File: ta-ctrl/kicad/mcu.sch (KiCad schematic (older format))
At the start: 11 parts, among them U6 MSP430FR5994IPM, Y1 32.768kHz, Y2 24MHz

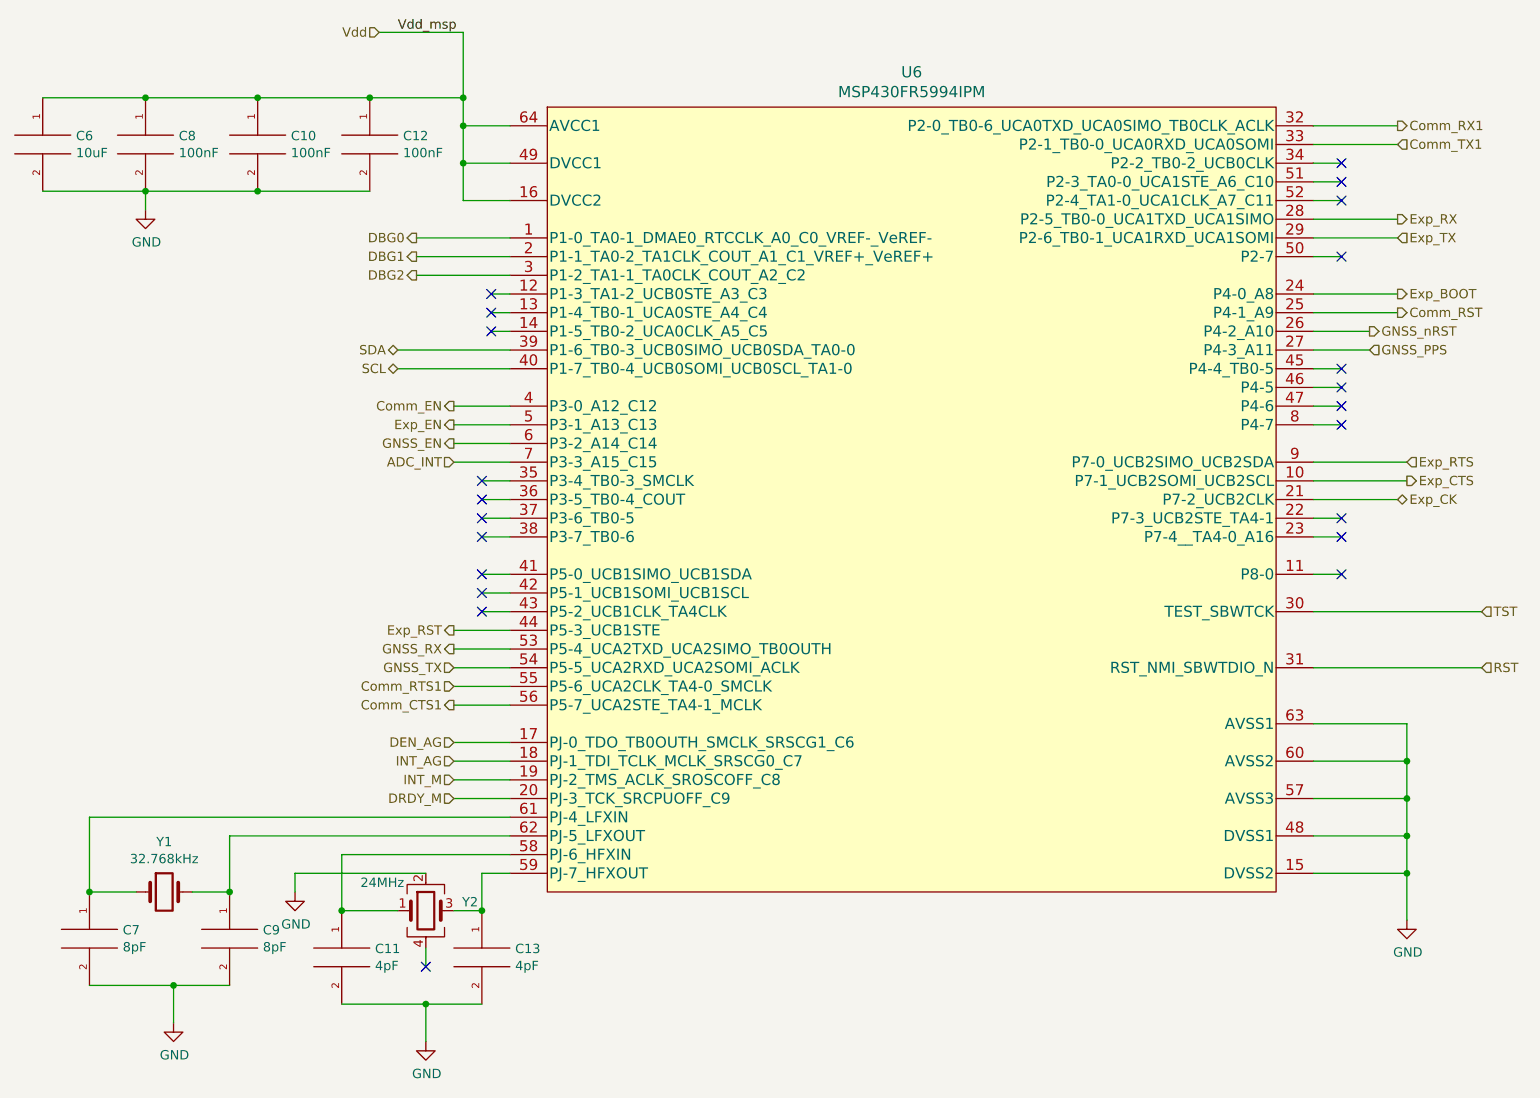
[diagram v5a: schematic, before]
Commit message: done routing except ground connections
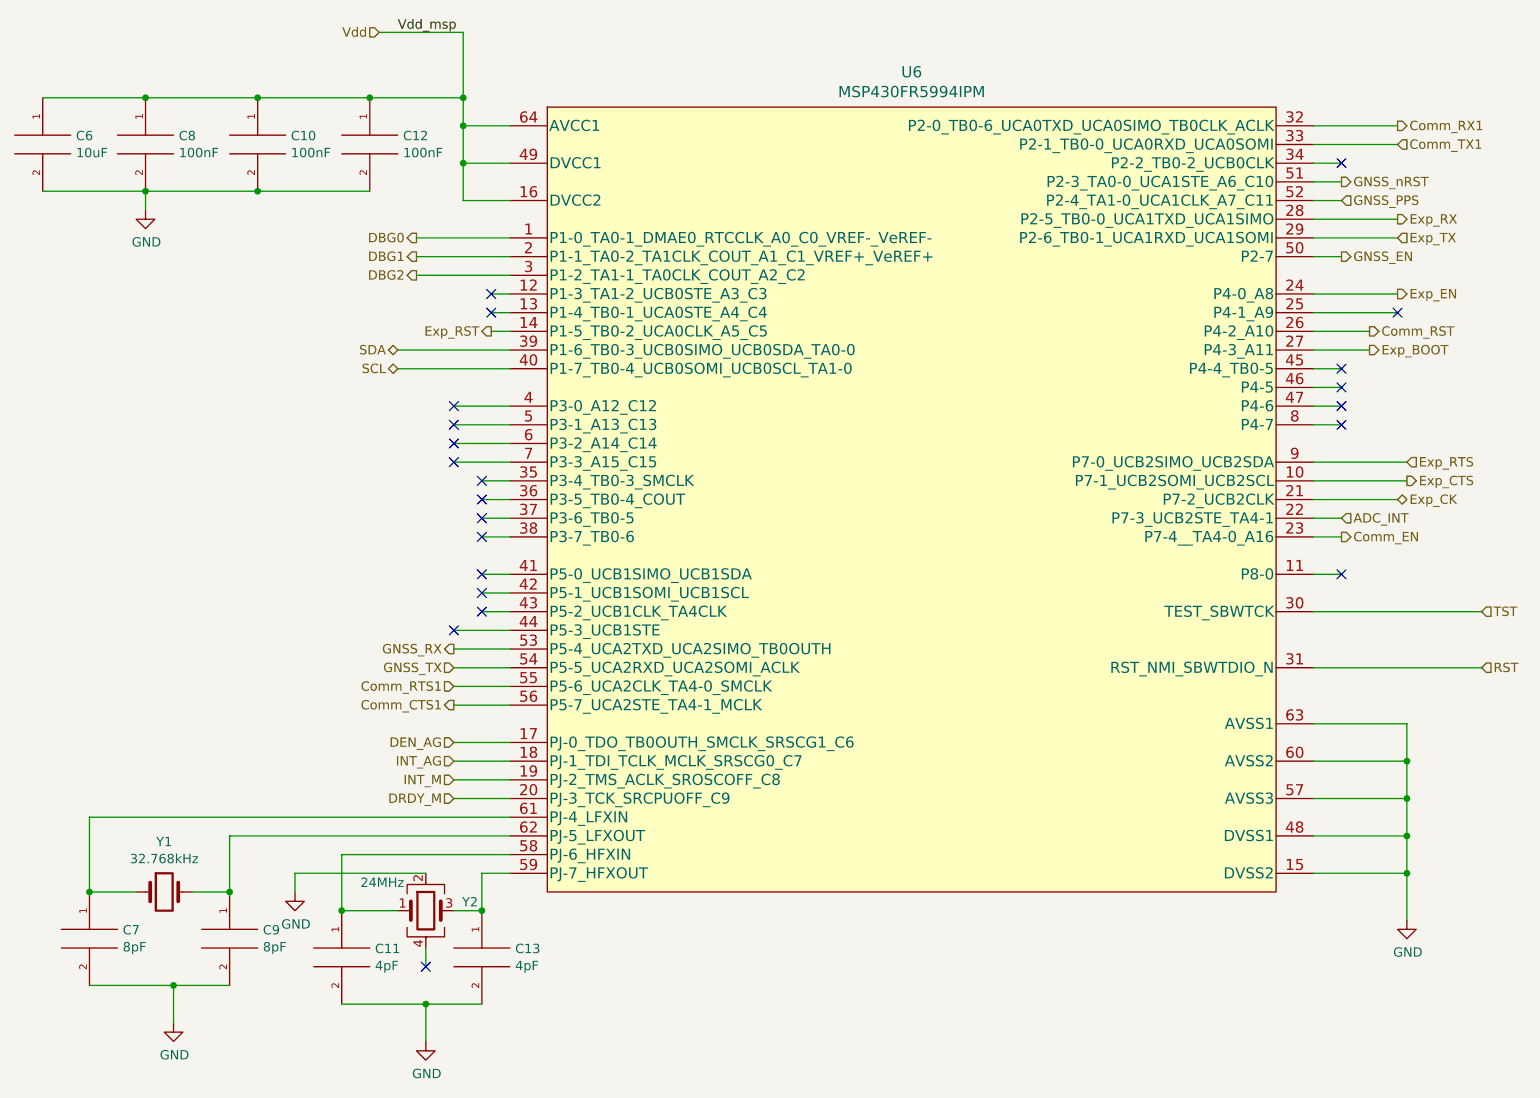
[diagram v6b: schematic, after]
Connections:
- net ADC_INT: now also U6.22 (P7-3_UCB2STE_TA4-1); no longer U6.7 (P3-3_A15_C15)
- net Comm_EN: now also U6.23 (P7-4__TA4-0_A16); no longer U6.4 (P3-0_A12_C12)
- net Comm_RST: now also U6.26 (P4-2_A10); no longer U6.25 (P4-1_A9)
- net Exp_BOOT: now also U6.27 (P4-3_A11); no longer U6.24 (P4-0_A8)
- net Exp_EN: now also U6.24 (P4-0_A8); no longer U6.5 (P3-1_A13_C13)
- net Exp_RST: now also U6.14 (P1-5_TB0-2_UCA0CLK_A5_C5); no longer U6.44 (P5-3_UCB1STE)
- net GNSS_EN: now also U6.50 (P2-7); no longer U6.6 (P3-2_A14_C14)
- net GNSS_PPS: now also U6.52 (P2-4_TA1-0_UCA1CLK_A7_C11); no longer U6.27 (P4-3_A11)
- net GNSS_nRST: now also U6.51 (P2-3_TA0-0_UCA1STE_A6_C10); no longer U6.26 (P4-2_A10)
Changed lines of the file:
@@
 Text HLabel 3050 4450 0    50   Input ~ 0
 GNSS_TX
-Text HLabel 7950 2650 2    50   Output ~ 0
+Text HLabel 7800 1850 2    50   Output ~ 0
 GNSS_nRST
-Text HLabel 7950 2750 2    50   Input ~ 0
+Text HLabel 7800 1950 2    50   Input ~ 0
 GNSS_PPS
 Text HLabel 2750 2750 0    50   BiDi ~ 0
@@
 Wire Wire Line
 	3050 4250 3350 4250
-Text HLabel 3050 3050 0    50   Output ~ 0
+Text HLabel 7800 3750 2    50   Output ~ 0
 Comm_EN
-Text HLabel 3050 3150 0    50   Output ~ 0
+Text HLabel 8100 2450 2    50   Output ~ 0
 Exp_EN
-Text HLabel 3050 3250 0    50   Output ~ 0
+Text HLabel 7800 2250 2    50   Output ~ 0
 GNSS_EN
 Wire Wire Line
@@
 Wire Wire Line
 	3050 3050 3350 3050
-Text HLabel 3050 3350 0    50   Input ~ 0
+Text HLabel 7800 3650 2    50   Input ~ 0
 ADC_INT
 Wire Wire Line
@@
 Wire Wire Line
 	3100 1750 3100 1950
-Text HLabel 8100 2450 2    50   Output ~ 0
+Text HLabel 7950 2750 2    50   Output ~ 0
 Exp_BOOT
-Text HLabel 8100 2550 2    50   Output ~ 0
+Text HLabel 7950 2650 2    50   Output ~ 0
 Comm_RST
 Wire Wire Line
@@
 Wire Wire Line
 	7650 2550 8100 2550
-Text HLabel 3050 4250 0    50   Output ~ 0
+Text HLabel 3250 2650 0    50   Output ~ 0
 Exp_RST
 Text HLabel 3050 5150 0    50   Input ~ 0
@@
 NoConn ~ 3250 2450
 NoConn ~ 3250 2550
-NoConn ~ 3250 2650
 Wire Wire Line
 	3250 2450 3350 2450
@@
 	3250 2650 3350 2650
 NoConn ~ 7800 1750
-NoConn ~ 7800 1850
-NoConn ~ 7800 1950
 Wire Wire Line
 	7650 1750 7800 1750
@@
 Wire Wire Line
 	7650 1950 7800 1950
-NoConn ~ 7800 2250
 Wire Wire Line
 	7650 2250 7800 2250
@@
 Wire Wire Line
 	7650 3150 7800 3150
-NoConn ~ 7800 3650
-NoConn ~ 7800 3750
 Wire Wire Line
 	7650 3650 7800 3650
@@
 Wire Wire Line
 	3350 3950 3200 3950
+NoConn ~ 3050 3250
+NoConn ~ 8100 2550
+NoConn ~ 3050 3050
+NoConn ~ 3050 3150
+NoConn ~ 3050 4250
+NoConn ~ 3050 3350
 $EndSCHEMATC

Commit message: updated parts vendors and added BOM
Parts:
- C10, C12, C8: Manufacturer Part Number (none) -> C0603C104K8RACAUTO; Vendor (none) -> Digikey; Vendor Part Number (none) -> 399-17574-1-ND
- C11, C13: Manufacturer Part Number (none) -> GJM1555C1H4R0BB01D; Vendor (none) -> Digikey; Vendor Part Number (none) -> 490-8100-1-ND
- C6: Manufacturer Part Number (none) -> C1608X7S0J106M080AC; Vendor (none) -> Digikey; Vendor Part Number (none) -> 445-9104-1-ND
- C7, C9: Manufacturer Part Number (none) -> GRM1555C1H8R0DA01D; Vendor (none) -> Digikey; Vendor Part Number (none) -> 490-5867-1-ND
- U6: Manufacturer Part Number (none) -> MSP430FR5994IPMR; Vendor (none) -> Digikey; Vendor Part Number (none) -> 296-45560-1-ND
- Y1: Manufacturer Part Number (none) -> ECS-.327-6-34QCS-TR; Vendor (none) -> Mouser; Vendor Part Number (none) -> 520-.327-6-34QCST
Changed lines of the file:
@@
 F 1 "MSP430FR5994IPM" H 5500 5731 60  0000 C CNN
 F 2 "ta-ctrl:MSP430FR5994IPM" H 5700 3490 60  0001 C CNN
-F 3 "" H 5700 3550 60  0000 C CNN
+F 3 "https://www.ti.com/lit/ds/symlink/msp430fr5994.pdf?HQS=TI-null-null-digikeymode-df-pf-null-wwe&ts=1595943774843" H 5700 3550 60  0001 C CNN
+F 4 "MSP430FR5994IPMR" H 5700 3550 50  0001 C CNN "Manufacturer Part Number"
+F 5 "Digikey" H 5700 3550 50  0001 C CNN "Vendor"
+F 6 "296-45560-1-ND" H 5700 3550 50  0001 C CNN "Vendor Part Number"
 	1    5700 3550
 	1    0    0    -1
@@
 F 1 "100nF" H 1578 1605 50  0000 L CNN
 F 2 "ta-ctrl:C_0603_1608Metric_ctrl_cpy" H 1400 1650 50  0001 C CNN
-F 3 "~" H 1400 1650 50  0001 C CNN
+F 3 "https://content.kemet.com/datasheets/KEM_C1023_X7R_AUTO_SMD.pdf" H 1400 1650 50  0001 C CNN
+F 4 "C0603C104K8RACAUTO" H 1400 1650 50  0001 C CNN "Manufacturer Part Number"
+F 5 "Digikey" H 1400 1650 50  0001 C CNN "Vendor"
+F 6 "399-17574-1-ND" H 1400 1650 50  0001 C CNN "Vendor Part Number"
 	1    1400 1650
 	1    0    0    -1
@@
 F 1 "100nF" H 2178 1605 50  0000 L CNN
 F 2 "ta-ctrl:C_0603_1608Metric_ctrl_cpy" H 2000 1650 50  0001 C CNN
-F 3 "~" H 2000 1650 50  0001 C CNN
+F 3 "https://content.kemet.com/datasheets/KEM_C1023_X7R_AUTO_SMD.pdf" H 2000 1650 50  0001 C CNN
+F 4 "C0603C104K8RACAUTO" H 2000 1650 50  0001 C CNN "Manufacturer Part Number"
+F 5 "Digikey" H 2000 1650 50  0001 C CNN "Vendor"
+F 6 "399-17574-1-ND" H 2000 1650 50  0001 C CNN "Vendor Part Number"
 	1    2000 1650
 	1    0    0    -1
@@
 F 1 "100nF" H 2778 1605 50  0000 L CNN
 F 2 "ta-ctrl:C_0603_1608Metric_ctrl_cpy" H 2600 1650 50  0001 C CNN
-F 3 "~" H 2600 1650 50  0001 C CNN
+F 3 "https://content.kemet.com/datasheets/KEM_C1023_X7R_AUTO_SMD.pdf" H 2600 1650 50  0001 C CNN
+F 4 "C0603C104K8RACAUTO" H 2600 1650 50  0001 C CNN "Manufacturer Part Number"
+F 5 "Digikey" H 2600 1650 50  0001 C CNN "Vendor"
+F 6 "399-17574-1-ND" H 2600 1650 50  0001 C CNN "Vendor Part Number"
 	1    2600 1650
 	1    0    0    -1
@@
 F 1 "10uF" H 1028 1605 50  0000 L CNN
 F 2 "ta-ctrl:C_0603_1608Metric_ctrl_cpy" H 850 1650 50  0001 C CNN
-F 3 "~" H 850 1650 50  0001 C CNN
+F 3 "https://product.tdk.com/info/en/catalog/datasheets/mlcc_commercial_general_en.pdf" H 850 1650 50  0001 C CNN
+F 4 "C1608X7S0J106M080AC" H 850 1650 50  0001 C CNN "Manufacturer Part Number"
+F 5 "Digikey" H 850 1650 50  0001 C CNN "Vendor"
+F 6 "445-9104-1-ND" H 850 1650 50  0001 C CNN "Vendor Part Number"
 	1    850  1650
 	1    0    0    -1
@@
 F 1 "8pF" H 2028 5855 50  0000 L CNN
 F 2 "ta-ctrl:C_0402_1005Metric" H 1850 5900 50  0001 C CNN
-F 3 "~" H 1850 5900 50  0001 C CNN
+F 3 "https://search.murata.co.jp/Ceramy/image/img/A01X/G101/ENG/GRM1555C1H8R0DA01-01.pdf" H 1850 5900 50  0001 C CNN
+F 4 "GRM1555C1H8R0DA01D" H 1850 5900 50  0001 C CNN "Manufacturer Part Number"
+F 5 "Digikey" H 1850 5900 50  0001 C CNN "Vendor"
+F 6 "490-5867-1-ND" H 1850 5900 50  0001 C CNN "Vendor Part Number"
 	1    1850 5900
 	1    0    0    -1
@@
 F 1 "8pF" H 1278 5855 50  0000 L CNN
 F 2 "ta-ctrl:C_0402_1005Metric" H 1100 5900 50  0001 C CNN
-F 3 "~" H 1100 5900 50  0001 C CNN
+F 3 "https://search.murata.co.jp/Ceramy/image/img/A01X/G101/ENG/GRM1555C1H8R0DA01-01.pdf" H 1100 5900 50  0001 C CNN
+F 4 "GRM1555C1H8R0DA01D" H 1100 5900 50  0001 C CNN "Manufacturer Part Number"
+F 5 "Digikey" H 1100 5900 50  0001 C CNN "Vendor"
+F 6 "490-5867-1-ND" H 1100 5900 50  0001 C CNN "Vendor Part Number"
 	1    1100 5900
 	1    0    0    -1
@@
 F 1 "4pF" H 3378 5955 50  0000 L CNN
 F 2 "ta-ctrl:C_0402_1005Metric" H 3200 6000 50  0001 C CNN
-F 3 "~" H 3200 6000 50  0001 C CNN
+F 3 "https://www.murata.com/~/media/webrenewal/support/library/catalog/products/capacitor/mlcc/c02e.ashx?la=en-us" H 3200 6000 50  0001 C CNN
+F 4 "GJM1555C1H4R0BB01D" H 3200 6000 50  0001 C CNN "Manufacturer Part Number"
+F 5 "Digikey" H 3200 6000 50  0001 C CNN "Vendor"
+F 6 "490-8100-1-ND" H 3200 6000 50  0001 C CNN "Vendor Part Number"
 	1    3200 6000
 	1    0    0    -1
@@
 F 1 "32.768kHz" H 1500 5827 50  0000 C CNN
 F 2 "ta-ctrl:ECS327934QSTR" H 1500 5650 50  0001 C CNN
-F 3 "~" H 1500 5650 50  0001 C CNN
+F 3 "https://www.mouser.com/datasheet/2/122/ECX-34Q-938174.pdf" H 1500 5650 50  0001 C CNN
+F 4 "ECS-.327-6-34QCS-TR" H 1500 5650 50  0001 C CNN "Manufacturer Part Number"
+F 5 "Mouser" H 1500 5650 50  0001 C CNN "Vendor"
+F 6 "520-.327-6-34QCST" H 1500 5650 50  0001 C CNN "Vendor Part Number"
 	1    1500 5650
 	1    0    0    -1
@@
 F 1 "4pF" H 2628 5955 50  0000 L CNN
 F 2 "ta-ctrl:C_0402_1005Metric" H 2450 6000 50  0001 C CNN
-F 3 "~" H 2450 6000 50  0001 C CNN
+F 3 "https://www.murata.com/~/media/webrenewal/support/library/catalog/products/capacitor/mlcc/c02e.ashx?la=en-us" H 2450 6000 50  0001 C CNN
+F 4 "GJM1555C1H4R0BB01D" H 2450 6000 50  0001 C CNN "Manufacturer Part Number"
+F 5 "Digikey" H 2450 6000 50  0001 C CNN "Vendor"
+F 6 "490-8100-1-ND" H 2450 6000 50  0001 C CNN "Vendor Part Number"
 	1    2450 6000
 	1    0    0    -1

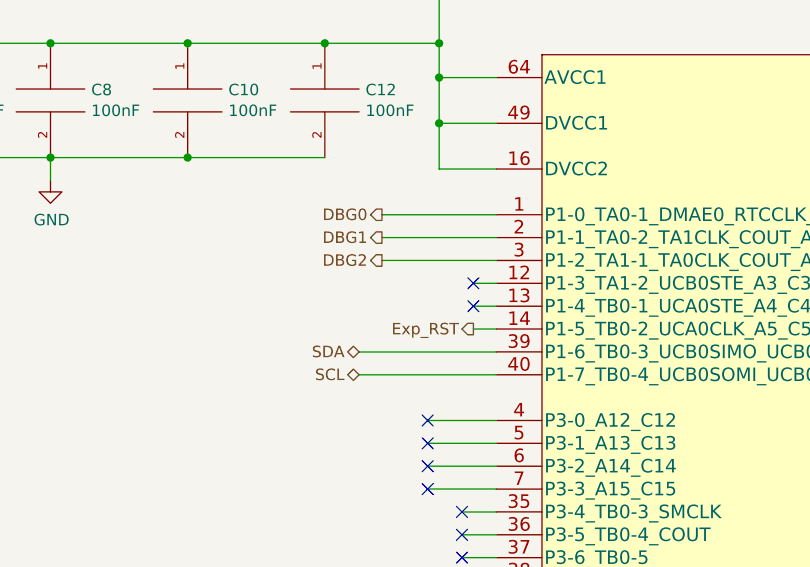
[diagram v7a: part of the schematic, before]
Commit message: deleted fp-info-cache files???
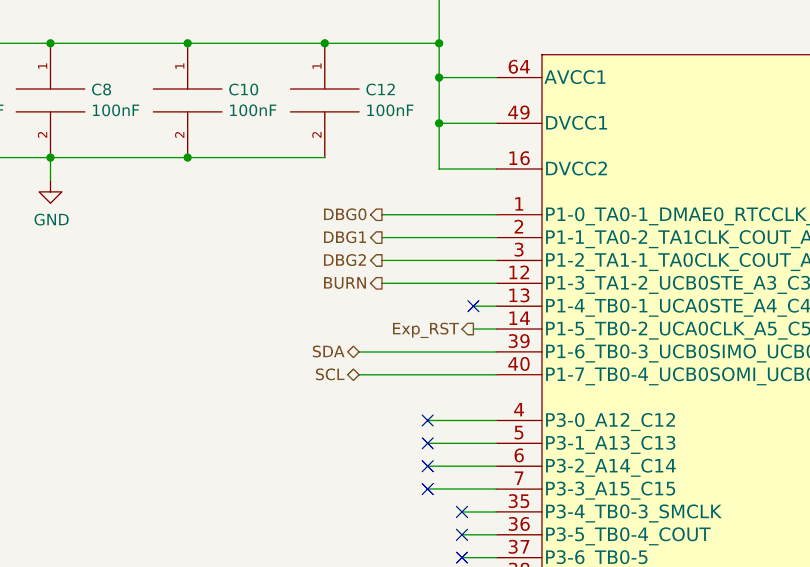
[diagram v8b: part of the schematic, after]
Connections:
- net BURN: now reaches U6.12 (P1-3_TA1-2_UCB0STE_A3_C3)
- no-connect marks 22 -> 21
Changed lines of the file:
@@
 Wire Wire Line
 	3200 3750 3350 3750
-NoConn ~ 3250 2450
 NoConn ~ 3250 2550
-Wire Wire Line
-	3250 2450 3350 2450
 Wire Wire Line
 	3250 2550 3350 2550
@@
 NoConn ~ 3050 4250
 NoConn ~ 3050 3350
+Text HLabel 2850 2450 0    50   Output ~ 0
+BURN
+Wire Wire Line
+	2850 2450 3350 2450
 $EndSCHEMATC
